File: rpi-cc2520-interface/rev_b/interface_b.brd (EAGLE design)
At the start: 30.5 x 39.5 mm, 11 parts, among them J1 PINHD-2X12/SMD, J2 PINHD-2X12/SMD

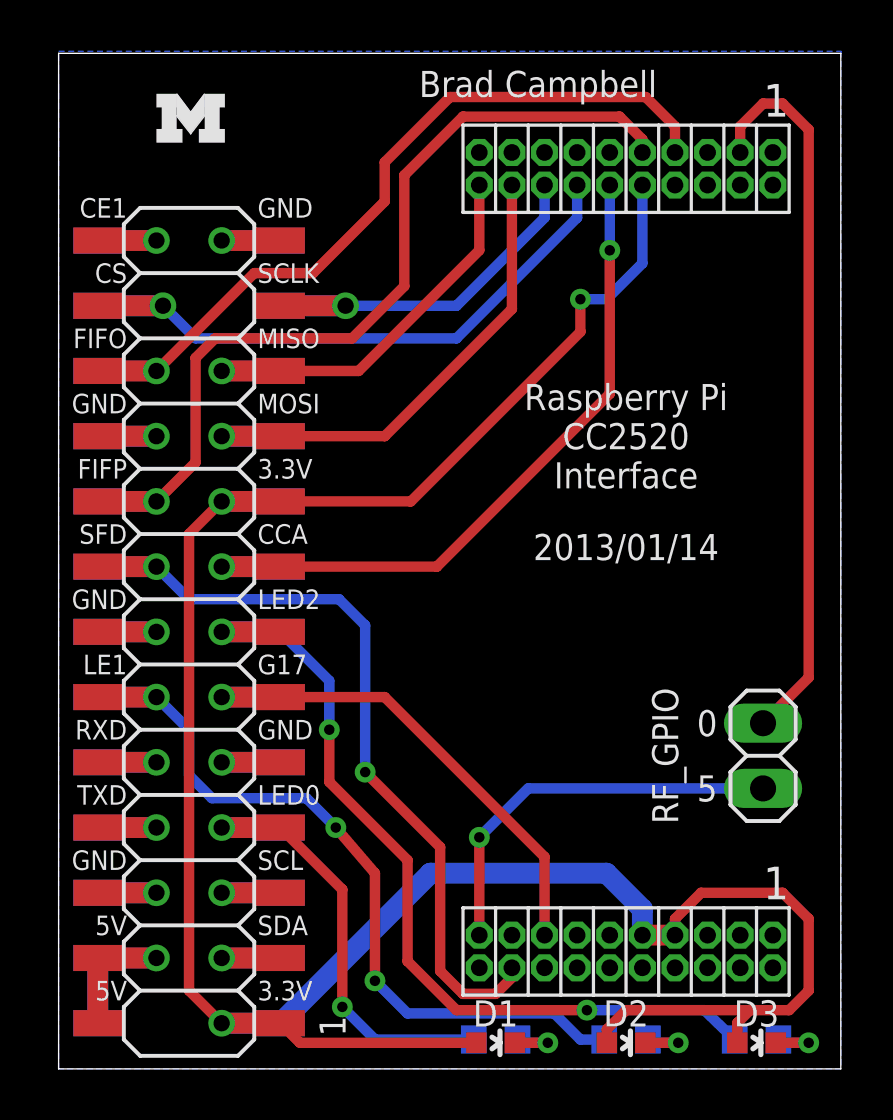
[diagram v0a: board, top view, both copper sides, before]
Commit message: moved some vias to make things nicer
git-svn-id: svn+ssh://energy.eecs.umich.edu/svnroot/shed/projects/pi-router/eagle@2768 d5a83394-2863-40c7-9603-03341d4c7fdc
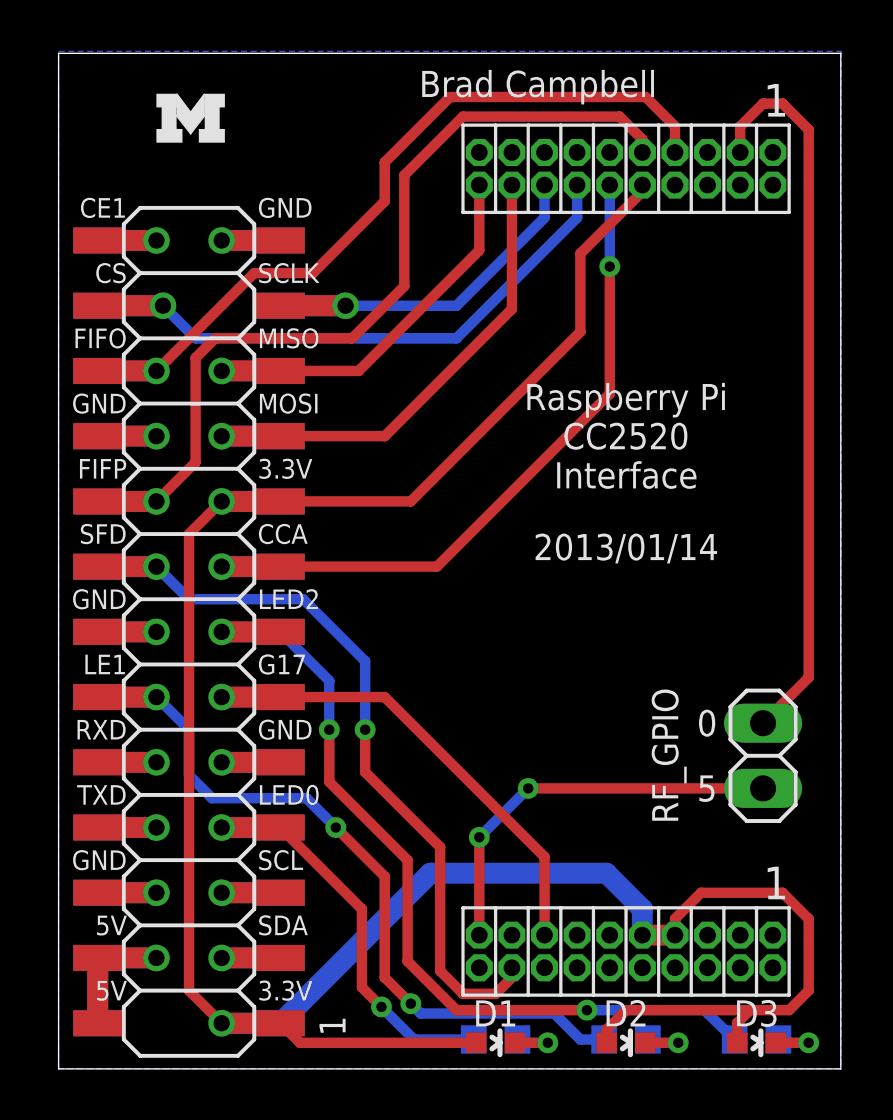
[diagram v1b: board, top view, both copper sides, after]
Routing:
- net LED0: track 18.2 -> 17.3 mm
- net SFD: track 32.1 -> 31.3 mm
- net VCC: track 99.5 -> 98.9 mm, vias 3 -> 2
- net CC_GPIO5: vias 1 -> 2
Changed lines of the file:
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@@
 <wire x1="8.636" y1="19.558" x2="6.35" y2="19.558" width="0.8128" layer="1"/>
 <wire x1="8.636" y1="19.558" x2="14.732" y2="19.558" width="0.4064" layer="1"/>
-<wire x1="21.463" y1="31.877" x2="21.463" y2="34.417" width="0.4064" layer="16"/>
-<via x="21.463" y="31.877" extent="1-16" drill="0.4064"/>
-<wire x1="21.463" y1="31.877" x2="21.463" y2="26.289" width="0.4064" layer="1"/>
+<wire x1="21.463" y1="31.242" x2="21.463" y2="34.417" width="0.4064" layer="16"/>
+<via x="21.463" y="31.242" extent="1-16" drill="0.4064"/>
+<wire x1="21.463" y1="31.242" x2="21.463" y2="26.289" width="0.4064" layer="1"/>
 <wire x1="21.463" y1="26.289" x2="14.732" y2="19.558" width="0.4064" layer="1"/>
 </signal>
@@
 <wire x1="3.81" y1="19.558" x2="1.524" y2="19.558" width="0.8128" layer="1"/>
 <wire x1="3.81" y1="19.558" x2="5.08" y2="18.288" width="0.4064" layer="16"/>
-<wire x1="5.08" y1="18.288" x2="10.922" y2="18.288" width="0.4064" layer="16"/>
-<wire x1="10.922" y1="18.288" x2="11.938" y2="17.272" width="0.4064" layer="16"/>
-<wire x1="11.938" y1="17.272" x2="11.938" y2="11.557" width="0.4064" layer="16"/>
-<via x="11.938" y="11.557" extent="1-16" drill="0.4064"/>
+<via x="11.938" y="13.208" extent="1-16" drill="0.4064"/>
+<wire x1="11.938" y1="13.208" x2="11.938" y2="11.557" width="0.4064" layer="1"/>
 <wire x1="11.938" y1="11.557" x2="14.859" y2="8.636" width="0.4064" layer="1"/>
 <wire x1="14.859" y1="8.636" x2="14.859" y2="3.81" width="0.4064" layer="1"/>
@@
 <wire x1="17.018" y1="2.921" x2="17.653" y2="3.556" width="0.4064" layer="1"/>
 <wire x1="17.653" y1="3.556" x2="17.653" y2="3.937" width="0.4064" layer="1"/>
+<wire x1="5.08" y1="18.288" x2="9.525" y2="18.288" width="0.4064" layer="16"/>
+<wire x1="9.525" y1="18.288" x2="11.938" y2="15.875" width="0.4064" layer="16"/>
+<wire x1="11.938" y1="15.875" x2="11.938" y2="13.208" width="0.4064" layer="16"/>
 </signal>
 <signal name="CC_GPIO5">
@@
 <via x="16.383" y="9.017" extent="1-16" drill="0.4064"/>
 <wire x1="16.383" y1="9.017" x2="18.288" y2="10.922" width="0.4064" layer="16"/>
-<wire x1="18.288" y1="10.922" x2="27.432" y2="10.922" width="0.4064" layer="16"/>
+<wire x1="18.288" y1="10.922" x2="27.432" y2="10.922" width="0.4064" layer="1"/>
+<via x="18.288" y="10.922" extent="1-16" drill="0.4064"/>
 </signal>
 <signal name="CC_GPIO0">
@@
 <wire x1="21.336" y1="7.62" x2="22.733" y2="6.223" width="0.8128" layer="16"/>
 <wire x1="22.733" y1="6.223" x2="22.733" y2="5.207" width="0.8128" layer="16"/>
-<via x="20.32" y="29.972" extent="1-16" drill="0.4064"/>
-<wire x1="20.32" y1="29.972" x2="21.336" y2="29.972" width="0.4064" layer="16"/>
-<wire x1="21.336" y1="29.972" x2="22.733" y2="31.369" width="0.4064" layer="16"/>
-<wire x1="22.733" y1="31.369" x2="22.733" y2="34.417" width="0.4064" layer="16"/>
 <wire x1="8.636" y1="22.098" x2="13.716" y2="22.098" width="0.4064" layer="1"/>
 <wire x1="13.716" y1="22.098" x2="20.32" y2="28.702" width="0.4064" layer="1"/>
-<wire x1="20.32" y1="28.702" x2="20.32" y2="29.972" width="0.4064" layer="1"/>
 <wire x1="8.636" y1="1.778" x2="6.35" y2="1.778" width="0.8128" layer="16"/>
 <wire x1="8.636" y1="1.778" x2="14.478" y2="7.62" width="0.8128" layer="16"/>
@@
 <wire x1="26.428" y1="1.016" x2="26.428" y2="1.79" width="0.4064" layer="1"/>
 <wire x1="26.428" y1="1.79" x2="26.924" y2="2.286" width="0.4064" layer="1"/>
-<wire x1="26.924" y1="2.286" x2="27.178" y2="2.286" width="0.4064" layer="1"/>
-<wire x1="27.178" y1="2.286" x2="28.448" y2="2.286" width="0.4064" layer="1"/>
+<wire x1="26.924" y1="2.286" x2="28.448" y2="2.286" width="0.4064" layer="1"/>
 <wire x1="28.448" y1="2.286" x2="29.21" y2="3.048" width="0.4064" layer="1"/>
 <wire x1="29.21" y1="3.048" x2="29.21" y2="5.842" width="0.4064" layer="1"/>
@@
 <wire x1="21.348" y1="1.536" x2="22.098" y2="2.286" width="0.4064" layer="1"/>
 <wire x1="22.098" y1="2.286" x2="26.924" y2="2.286" width="0.4064" layer="1"/>
+<wire x1="20.32" y1="28.702" x2="20.32" y2="31.75" width="0.4064" layer="1"/>
+<wire x1="20.32" y1="31.75" x2="22.733" y2="34.163" width="0.4064" layer="1"/>
+<wire x1="22.733" y1="34.163" x2="22.733" y2="34.417" width="0.4064" layer="1"/>
 </signal>
 <signal name="LED2">
@@
 <via x="3.81" y="14.478" extent="1-16" drill="0.635"/>
 <wire x1="3.81" y1="14.478" x2="1.524" y2="14.478" width="0.8128" layer="1"/>
-<wire x1="13.589" y1="2.159" x2="12.319" y2="3.429" width="0.4064" layer="16"/>
-<via x="12.319" y="3.429" extent="1-16" drill="0.4064"/>
-<wire x1="12.319" y1="3.429" x2="12.319" y2="7.62" width="0.4064" layer="1"/>
-<wire x1="12.319" y1="7.62" x2="10.795" y2="9.398" width="0.4064" layer="1"/>
+<wire x1="14.097" y1="2.159" x2="13.716" y2="2.54" width="0.4064" layer="16"/>
+<via x="13.716" y="2.54" extent="1-16" drill="0.4064"/>
+<wire x1="13.716" y1="2.54" x2="12.7" y2="3.556" width="0.4064" layer="1"/>
+<wire x1="12.7" y1="3.556" x2="12.7" y2="7.493" width="0.4064" layer="1"/>
+<wire x1="12.7" y1="7.493" x2="10.795" y2="9.398" width="0.4064" layer="1"/>
 <via x="10.795" y="9.398" extent="1-16" drill="0.4064"/>
 <wire x1="10.795" y1="9.398" x2="9.652" y2="10.541" width="0.4064" layer="16"/>
@@
 <wire x1="21.248" y1="1.143" x2="20.32" y2="1.143" width="0.4064" layer="16"/>
 <wire x1="20.32" y1="1.143" x2="19.304" y2="2.159" width="0.4064" layer="16"/>
-<wire x1="19.304" y1="2.159" x2="13.589" y2="2.159" width="0.4064" layer="16"/>
+<wire x1="19.304" y1="2.159" x2="14.097" y2="2.159" width="0.4064" layer="16"/>
 </signal>
 <signal name="LED0">
@@
 <via x="6.35" y="9.398" extent="1-16" drill="0.635"/>
 <wire x1="6.35" y1="9.398" x2="8.636" y2="9.398" width="0.8128" layer="16"/>
-<wire x1="11.049" y1="2.413" x2="11.049" y2="6.985" width="0.4064" layer="1"/>
-<wire x1="11.049" y1="6.985" x2="8.636" y2="9.398" width="0.4064" layer="1"/>
-<wire x1="16.168" y1="1.143" x2="12.319" y2="1.143" width="0.4064" layer="16"/>
-<wire x1="12.319" y1="1.143" x2="11.049" y2="2.413" width="0.4064" layer="16"/>
-<via x="11.049" y="2.413" extent="1-16" drill="0.4064"/>
+<wire x1="12.573" y1="2.413" x2="11.811" y2="3.175" width="0.4064" layer="1"/>
+<wire x1="11.811" y1="3.175" x2="11.811" y2="6.223" width="0.4064" layer="1"/>
+<wire x1="11.811" y1="6.223" x2="8.636" y2="9.398" width="0.4064" layer="1"/>
+<wire x1="16.168" y1="1.143" x2="13.843" y2="1.143" width="0.4064" layer="16"/>
+<wire x1="13.843" y1="1.143" x2="12.573" y2="2.413" width="0.4064" layer="16"/>
+<via x="12.573" y="2.413" extent="1-16" drill="0.4064"/>
 </signal>
 </signals>
